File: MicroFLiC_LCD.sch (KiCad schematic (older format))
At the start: 18 parts, among them P1 2x8 pin header, P2 1x16 pin header, P3 1x16 pin socket, Q1 BCX54-16, U1 MCP4728, U2 TLV2371

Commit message: Renamed files, added part description
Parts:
- A1: value Arduino Micro -> Arduino MICRO; Alt. Order Code (none) -> Arduino MICRO; Alt. Supplier (none) -> Arduino.cc; Note (none) -> Arduino/Genuino MICRO development board; Package (none) -> Arduino MICRO; Supplier (none) -> Farnell
- C1: value 10u -> 10u/10V; Alt. Order Code (none) -> 81-GRM21BR61A106KE19; Alt. Supplier (none) -> Mouser; Note (none) -> 10μF/10V X5R 0805 ceramic capacitor; Package (none) -> 0805; Supplier (none) -> Farnell
- C2, C3: Alt. Order Code (none) -> 710-885012207098; Alt. Supplier (none) -> Mouser; Note (none) -> 100nF/50V X7R 0805 ceramic capacitor; Package (none) -> 0805; Supplier (none) -> Farnell
- LCD1: Alt. Order Code (none) -> 763-0420DZ-FL-YBW; Alt. Supplier (none) -> Mouser; Note (none) -> 20x4 character liquid crystal display; Package (none) -> 98x60mm; Supplier (none) -> Farnell
- P1: value 2x8 pin header -> 2x8 header strip; Note 2x8 pin header -> 2x8 dual header strip
- P2: value 1x16 pin header -> 1x16 header strip; Manufacturer Werth Elektronik -> Wurth Elektronik
- P3: value 1x16 pin socket -> 1x16 socket strip
- Q1: Alt. Order Code (none) -> 771-BCX54-16-T/R; Alt. Supplier (none) -> Mouser; Manufacturer NXP -> NXP Semiconductors; Note (none) -> Bipolar SOT-89 NPN transistor; Package (none) -> SOT-89; Supplier (none) -> Farnell
- R1: Alt. Order Code (none) -> 71-CRCW0805-10K-E3; Alt. Supplier (none) -> Mouser; Note (none) -> 10kΩ/1% 0805 resistor; Package (none) -> 0805; Supplier (none) -> Farnell
- R2, R3: value 18R(0.25W) -> 18R(0.5W); Alt. Order Code (none) -> 667-ERJ-P6WF18R0V; Alt. Supplier (none) -> Mouser; Note (none) -> 18Ω/1%/500mW 0805 resistor; Package (none) -> 0805; Supplier (none) -> Farnell
- U1: Alt. Order Code (none) -> 579-MCP4728-E/UN; Alt. Supplier (none) -> Mouser; Note (none) -> 12-bit quad digital-to-analog converter with EEPROM memory; Package (none) -> MSOP-10; Supplier (none) -> Farnell
- U2: Alt. Order Code (none) -> 595-TLV2371IDBVT; Alt. Supplier (none) -> Mouser; Note (none) -> 3 MHz rail-to-rail input/output operational amplifier; Package (none) -> SOT-23-5; Supplier (none) -> Farnell
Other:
- moved on the sheet: C1
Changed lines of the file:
@@
 LIBS:valves
 LIBS:jakub
-LIBS:MicroFLiC_LCD_1_0-cache
+LIBS:MicroFLiC_LCD-cache
 EELAYER 25 0
 EELAYER END
@@
 P 6100 2300
 F 0 "A1" H 6100 3300 60  0000 C CNN
-F 1 "Arduino Micro" V 6100 2300 60  0000 C CNN
+F 1 "Arduino MICRO" V 6100 2300 60  0000 C CNN
 F 2 "jakub:ArduinoMicro" V 5350 2750 60  0001 C CNN
 F 3 "" V 5350 2750 60  0000 C CNN
 F 4 "A000053" H 6100 2300 60  0001 C CNN "Part Number"
 F 5 "Arduino" H 6100 2300 60  0001 C CNN "Manufacturer"
-F 6 "2285194" H 6100 2300 60  0001 C CNN "Order Code"
+F 6 "Arduino MICRO" H 6100 2300 60  0001 C CNN "Package"
+F 7 "Farnell" H 6100 2300 60  0001 C CNN "Supplier"
+F 8 "2285194" H 6100 2300 60  0001 C CNN "Order Code"
+F 9 "Arduino.cc" H 6100 2300 60  0001 C CNN "Alt. Supplier"
+F 10 "Arduino MICRO" H 6100 2300 60  0001 C CNN "Alt. Order Code"
+F 11 "Arduino/Genuino MICRO development board" H 6100 2300 60  0001 C CNN "Note"
 	1    6100 2300
 	1    0    0    -1
@@
 P 1550 2050
 F 0 "P1" H 1550 2500 50  0000 C CNN
-F 1 "2x8 pin header" V 1550 2050 50  0000 C CNN
+F 1 "2x8 header strip" V 1550 2050 50  0000 C CNN
 F 2 "Pin_Headers:Pin_Header_Straight_2x08" H 1550 850 50  0001 C CNN
 F 3 "" H 1550 850 50  0000 C CNN
@@
 F 9 "Mouser" H 1550 2050 60  0001 C CNN "Alt. Supplier"
 F 10 "855-M20-9980845" H 1550 2050 60  0001 C CNN "Alt. Order Code"
-F 11 "2x8 pin header" H 1550 2050 60  0001 C CNN "Note"
+F 11 "2x8 dual header strip" H 1550 2050 60  0001 C CNN "Note"
 	1    1550 2050
 	1    0    0    -1
@@
 F 4 "MC42005A12W-VNMLR" H 9800 2250 60  0001 C CNN "Part Number"
 F 5 "Midas" H 9800 2250 60  0001 C CNN "Manufacturer"
-F 6 "2483355" H 9800 2250 60  0001 C CNN "Order Code"
+F 6 "98x60mm" H 9800 2250 60  0001 C CNN "Package"
+F 7 "Farnell" H 9800 2250 60  0001 C CNN "Supplier"
+F 8 "2483355" H 9800 2250 60  0001 C CNN "Order Code"
+F 9 "Mouser" H 9800 2250 60  0001 C CNN "Alt. Supplier"
+F 10 "763-0420DZ-FL-YBW" H 9800 2250 60  0001 C CNN "Alt. Order Code"
+F 11 "20x4 character liquid crystal display" H 9800 2250 60  0001 C CNN "Note"
 	1    9800 2250
 	1    0    0    -1
@@
 F 4 "MCP4728-E/UN" H 5800 4800 60  0001 C CNN "Part Number"
 F 5 "Microchip" H 5800 4800 60  0001 C CNN "Manufacturer"
-F 6 "1800217" H 5800 4800 60  0001 C CNN "Order Code"
+F 6 "MSOP-10" H 5800 4800 60  0001 C CNN "Package"
+F 7 "Farnell" H 5800 4800 60  0001 C CNN "Supplier"
+F 8 "1800217" H 5800 4800 60  0001 C CNN "Order Code"
+F 9 "Mouser" H 5800 4800 60  0001 C CNN "Alt. Supplier"
+F 10 "579-MCP4728-E/UN" H 5800 4800 60  0001 C CNN "Alt. Order Code"
+F 11 "12-bit quad digital-to-analog converter with EEPROM memory" H 5800 4800 60  0001 C CNN "Note"
 	1    5800 4800
 	1    0    0    -1
@@
 F 4 "MC0805B104K250CT" H 4800 5450 60  0001 C CNN "Part Number"
 F 5 "Multicomp" H 4800 5450 60  0001 C CNN "Manufacturer"
-F 6 "1759166" H 4800 5450 60  0001 C CNN "Order Code"
+F 6 "0805" H 4800 5450 60  0001 C CNN "Package"
+F 7 "Farnell" H 4800 5450 60  0001 C CNN "Supplier"
+F 8 "1759166" H 4800 5450 60  0001 C CNN "Order Code"
+F 9 "Mouser" H 4800 5450 60  0001 C CNN "Alt. Supplier"
+F 10 "710-885012207098" H 4800 5450 60  0001 C CNN "Alt. Order Code"
+F 11 "100nF/50V X7R 0805 ceramic capacitor" H 4800 5450 60  0001 C CNN "Note"
 	1    4800 5450
 	1    0    0    -1
@@
 L C C1
 U 1 1 566AEC7D
-P 4500 5450
-F 0 "C1" H 4525 5550 50  0000 L CNN
-F 1 "10u" H 4525 5350 50  0000 L CNN
-F 2 "Capacitors_SMD:C_0805" H 4538 5300 50  0001 C CNN
-F 3 "" H 4500 5450 50  0000 C CNN
-F 4 "GRM21BR61A106KE19L" H 4500 5450 60  0001 C CNN "Part Number"
-F 5 "Murata" H 4500 5450 60  0001 C CNN "Manufacturer"
-F 6 "1828805" H 4500 5450 60  0001 C CNN "Order Code"
-	1    4500 5450
-	1    0    0    -1
-$EndComp
-Wire Wire Line
-	4500 5800 5700 5800
+P 4300 5450
+F 0 "C1" H 4325 5550 50  0000 L CNN
+F 1 "10u/10V" H 4325 5350 50  0000 L CNN
+F 2 "Capacitors_SMD:C_0805" H 4338 5300 50  0001 C CNN
+F 3 "" H 4300 5450 50  0000 C CNN
+F 4 "GRM21BR61A106KE19L" H 4300 5450 60  0001 C CNN "Part Number"
+F 5 "Murata" H 4300 5450 60  0001 C CNN "Manufacturer"
+F 6 "0805" H 4300 5450 60  0001 C CNN "Package"
+F 7 "Farnell" H 4300 5450 60  0001 C CNN "Supplier"
+F 8 "1828805" H 4300 5450 60  0001 C CNN "Order Code"
+F 9 "Mouser" H 4300 5450 60  0001 C CNN "Alt. Supplier"
+F 10 "81-GRM21BR61A106KE19" H 4300 5450 60  0001 C CNN "Alt. Order Code"
+F 11 "10μF/10V X5R 0805 ceramic capacitor" H 4300 5450 60  0001 C CNN "Note"
+	1    4300 5450
+	1    0    0    -1
+$EndComp
+Wire Wire Line
+	4300 5800 5700 5800
 Wire Wire Line
 	4800 5800 4800 5600
@@
 	5700 5800 5800 5700
 Wire Wire Line
-	4500 5300 4500 5200
-Wire Wire Line
-	4500 5200 4800 5200
+	4300 5300 4300 5200
+Wire Wire Line
+	4300 5200 4800 5200
 Connection ~ 4800 5200
 Wire Wire Line
-	4500 5600 4500 5800
+	4300 5600 4300 5800
 Connection ~ 4800 5800
 Wire Wire Line
@@
 F 4 "MCMR08X1002FTL" V 6850 4650 60  0001 C CNN "Part Number"
 F 5 "Multicomp" V 6850 4650 60  0001 C CNN "Manufacturer"
-F 6 "2073607" V 6850 4650 60  0001 C CNN "Order Code"
+F 6 "0805" H 6850 4650 60  0001 C CNN "Package"
+F 7 "Farnell" H 6850 4650 60  0001 C CNN "Supplier"
+F 8 "2073607" V 6850 4650 60  0001 C CNN "Order Code"
+F 9 "Mouser" H 6850 4650 60  0001 C CNN "Alt. Supplier"
+F 10 "71-CRCW0805-10K-E3" H 6850 4650 60  0001 C CNN "Alt. Order Code"
+F 11 "10kΩ/1% 0805 resistor" H 6850 4650 60  0001 C CNN "Note"
 	1    6850 4650
 	0    1    1    0
@@
 F 4 "TLV2371IDBVT" H 9000 4700 60  0001 C CNN "Part Number"
 F 5 "Texas Instruments" H 9000 4700 60  0001 C CNN "Manufacturer"
-F 6 "8454990" H 9000 4700 60  0001 C CNN "Order Code"
+F 6 "SOT-23-5" H 9000 4700 60  0001 C CNN "Package"
+F 7 "Farnell" H 9000 4700 60  0001 C CNN "Supplier"
+F 8 "8454990" H 9000 4700 60  0001 C CNN "Order Code"
+F 9 "Mouser" H 9000 4700 60  0001 C CNN "Alt. Supplier"
+F 10 "595-TLV2371IDBVT" H 9000 4700 60  0001 C CNN "Alt. Order Code"
+F 11 "3 MHz rail-to-rail input/output operational amplifier" H 9000 4700 60  0001 C CNN "Note"
 	1    9000 4700
 	1    0    0    -1
@@
 P 10000 5250
 F 0 "R2" H 10050 5300 50  0000 L CNN
-F 1 "18R(0.25W)" H 10050 5200 50  0000 L CNN
+F 1 "18R(0.5W)" H 10050 5200 50  0000 L CNN
 F 2 "Resistors_SMD:R_0805" V 9930 5250 50  0001 C CNN
 F 3 "" H 10000 5250 50  0000 C CNN
 F 4 "ERJP6WF18R0V" H 10000 5250 60  0001 C CNN "Part Number"
 F 5 "Panasonic" H 10000 5250 60  0001 C CNN "Manufacturer"
-F 6 "2253864" H 10000 5250 60  0001 C CNN "Order Code"
+F 6 "0805" H 10000 5250 60  0001 C CNN "Package"
+F 7 "Farnell" H 10000 5250 60  0001 C CNN "Supplier"
+F 8 "2253864" H 10000 5250 60  0001 C CNN "Order Code"
+F 9 "Mouser" H 10000 5250 60  0001 C CNN "Alt. Supplier"
+F 10 "667-ERJ-P6WF18R0V" H 10000 5250 60  0001 C CNN "Alt. Order Code"
+F 11 "18Ω/1%/500mW 0805 resistor" H 10000 5250 60  0001 C CNN "Note"
 	1    10000 5250
 	1    0    0    -1
@@
 F 3 "" H 9900 4700 50  0000 C CNN
 F 4 "BCX54-16" H 9900 4700 60  0001 C CNN "Part Number"
-F 5 "NXP" H 9900 4700 60  0001 C CNN "Manufacturer"
-F 6 "8734950" H 9900 4700 60  0001 C CNN "Order Code"
+F 5 "NXP Semiconductors" H 9900 4700 60  0001 C CNN "Manufacturer"
+F 6 "SOT-89" H 9900 4700 60  0001 C CNN "Package"
+F 7 "Farnell" H 9900 4700 60  0001 C CNN "Supplier"
+F 8 "8734950" H 9900 4700 60  0001 C CNN "Order Code"
+F 9 "Mouser" H 9900 4700 60  0001 C CNN "Alt. Supplier"
+F 10 "771-BCX54-16-T/R" H 9900 4700 60  0001 C CNN "Alt. Order Code"
+F 11 "Bipolar SOT-89 NPN transistor" H 9900 4700 60  0001 C CNN "Note"
 	1    9900 4700
 	1    0    0    -1
@@
 F 4 "MC0805B104K250CT" H 8100 4850 60  0001 C CNN "Part Number"
 F 5 "Multicomp" H 8100 4850 60  0001 C CNN "Manufacturer"
-F 6 "1759166" H 8100 4850 60  0001 C CNN "Order Code"
+F 6 "0805" H 8100 4850 60  0001 C CNN "Package"
+F 7 "Farnell" H 8100 4850 60  0001 C CNN "Supplier"
+F 8 "1759166" H 8100 4850 60  0001 C CNN "Order Code"
+F 9 "Mouser" H 8100 4850 60  0001 C CNN "Alt. Supplier"
+F 10 "710-885012207098" H 8100 4850 60  0001 C CNN "Alt. Order Code"
+F 11 "100nF/50V X7R 0805 ceramic capacitor" H 8100 4850 60  0001 C CNN "Note"
 	1    8100 4850
 	1    0    0    -1
@@
 P 10000 5650
 F 0 "R3" H 10050 5700 50  0000 L CNN
-F 1 "18R(0.25W)" H 10050 5600 50  0000 L CNN
+F 1 "18R(0.5W)" H 10050 5600 50  0000 L CNN
 F 2 "Resistors_SMD:R_0805" V 9930 5650 50  0001 C CNN
 F 3 "" H 10000 5650 50  0000 C CNN
 F 4 "ERJP6WF18R0V" H 10000 5650 60  0001 C CNN "Part Number"
 F 5 "Panasonic" H 10000 5650 60  0001 C CNN "Manufacturer"
-F 6 "2253864" H 10000 5650 60  0001 C CNN "Order Code"
+F 6 "0805" H 10000 5650 60  0001 C CNN "Package"
+F 7 "Farnell" H 10000 5650 60  0001 C CNN "Supplier"
+F 8 "2253864" H 10000 5650 60  0001 C CNN "Order Code"
+F 9 "Mouser" H 10000 5650 60  0001 C CNN "Alt. Supplier"
+F 10 "667-ERJ-P6WF18R0V" H 10000 5650 60  0001 C CNN "Alt. Order Code"
+F 11 "18Ω/1%/500mW 0805 resistor" H 10000 5650 60  0001 C CNN "Note"
 	1    10000 5650
 	1    0    0    -1
@@
 P 10600 2250
 F 0 "P2" H 10600 3100 50  0000 C CNN
-F 1 "1x16 pin header" V 10700 2250 50  0000 C CNN
+F 1 "1x16 header strip" V 10700 2250 50  0000 C CNN
 F 2 "" H 10600 2250 50  0000 C CNN
 F 3 "" H 10600 2250 50  0000 C CNN
 F 4 "61301611121" H 10600 2250 60  0001 C CNN "Part Number"
-F 5 "Werth Elektronik" H 10600 2250 60  0001 C CNN "Manufacturer"
+F 5 "Wurth Elektronik" H 10600 2250 60  0001 C CNN "Manufacturer"
 F 6 "SIL-16" H 10600 2250 60  0001 C CNN "Package"
 F 7 "Farnell" H 10600 2250 60  0001 C CNN "Supplier"
@@
 P 11000 2250
 F 0 "P3" H 11000 3100 50  0000 C CNN
-F 1 "1x16 pin socket" V 11100 2250 50  0000 C CNN
+F 1 "1x16 socket strip" V 11100 2250 50  0000 C CNN
 F 2 "" H 11000 2250 50  0000 C CNN
 F 3 "" H 11000 2250 50  0000 C CNN

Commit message: Fixed LCD part description
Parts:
- LCD1: Package 98x60mm -> 98mm×60mm
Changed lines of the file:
@@
 F 4 "MC42005A12W-VNMLR" H 9800 2250 60  0001 C CNN "Part Number"
 F 5 "Midas" H 9800 2250 60  0001 C CNN "Manufacturer"
-F 6 "98x60mm" H 9800 2250 60  0001 C CNN "Package"
+F 6 "98mm×60mm" H 9800 2250 60  0001 C CNN "Package"
 F 7 "Farnell" H 9800 2250 60  0001 C CNN "Supplier"
 F 8 "2483355" H 9800 2250 60  0001 C CNN "Order Code"

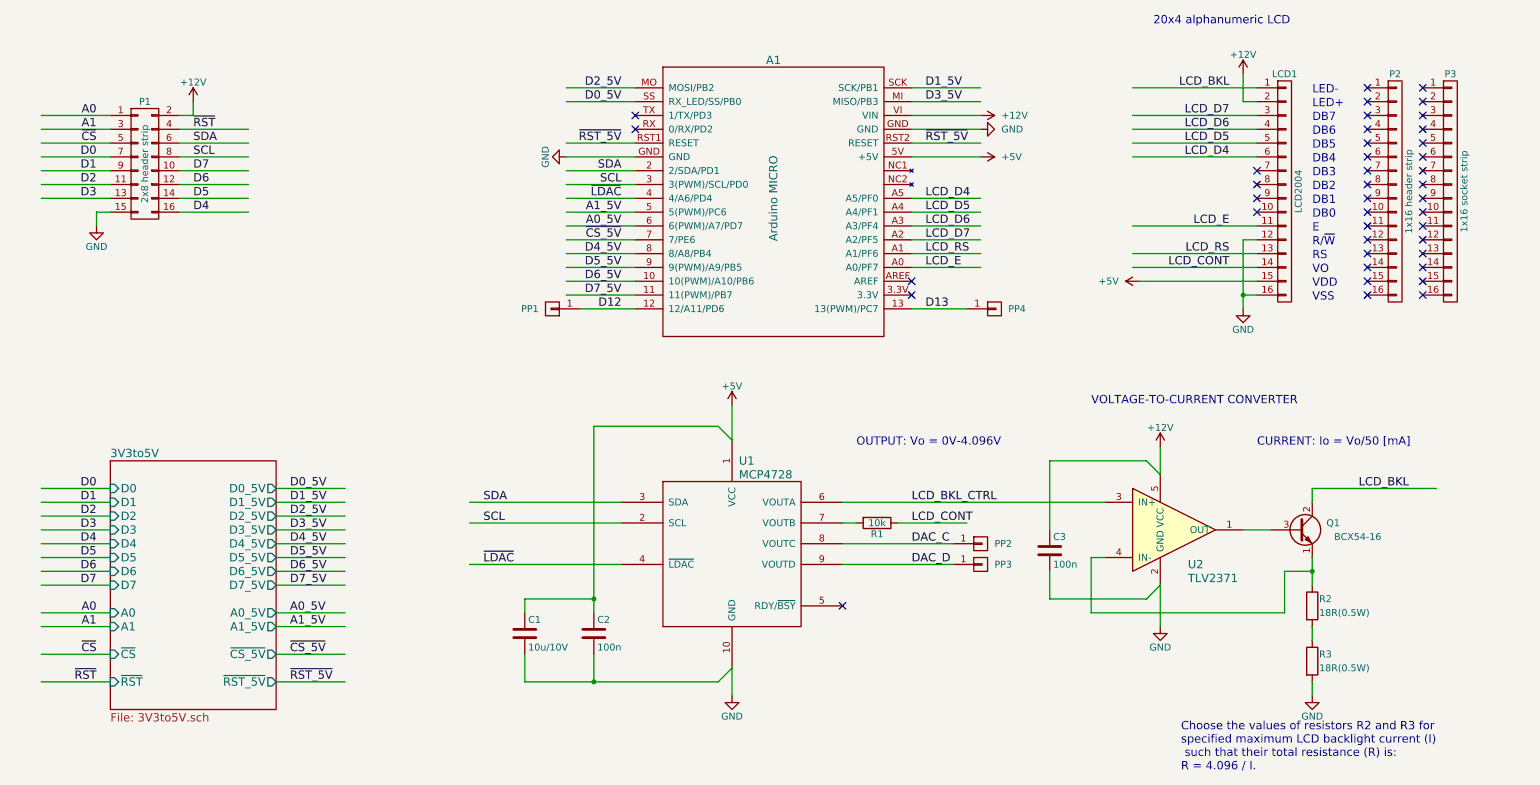
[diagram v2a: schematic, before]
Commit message: Fixed LCD orientation, added powerful emitter-follower amplifier
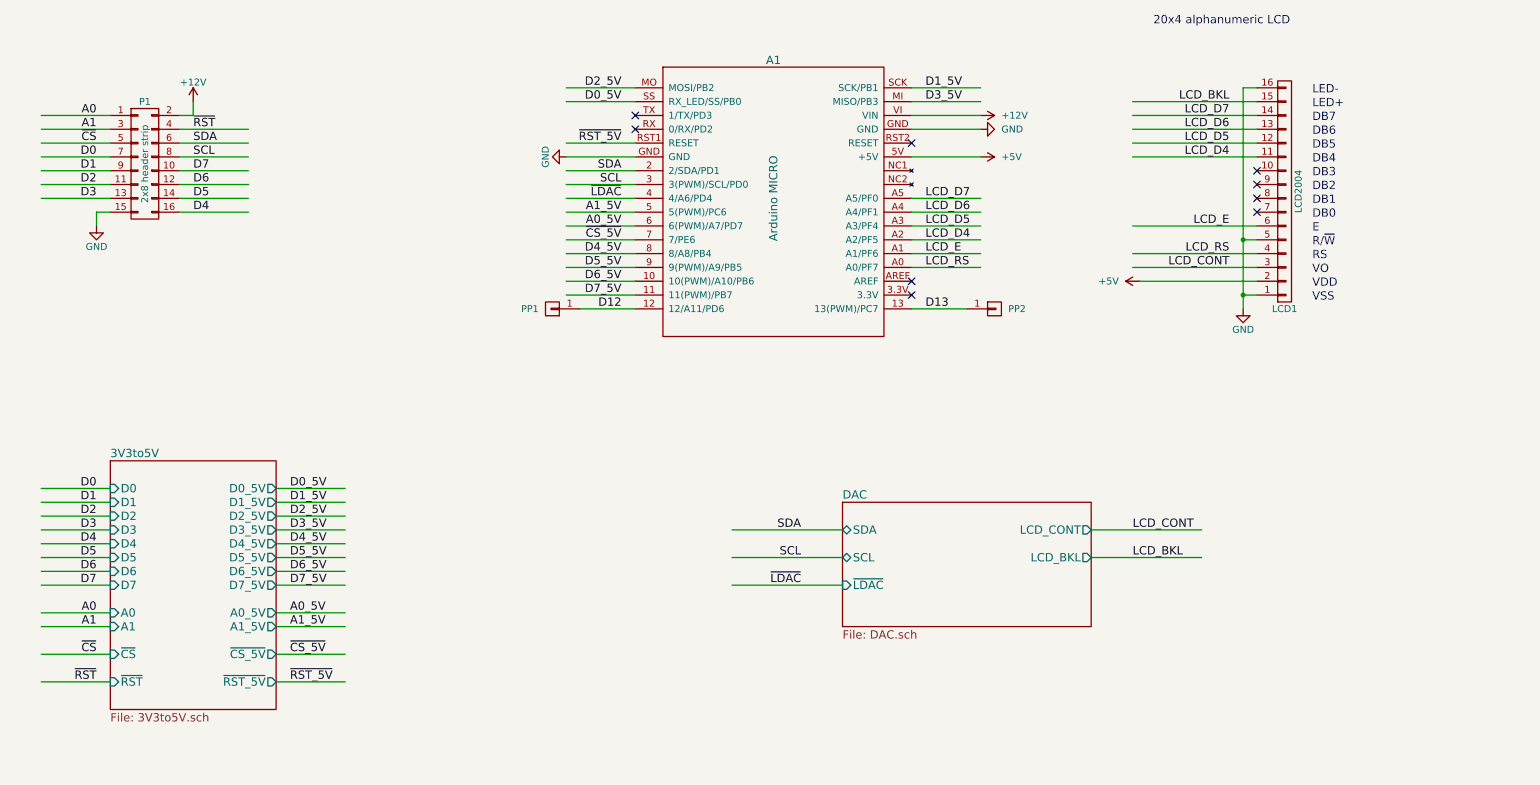
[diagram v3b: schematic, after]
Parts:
- removed C1: 10u/10V, Capacitors_SMD:C_0805, symbol C
- removed C2, C3: 100n, Capacitors_SMD:C_0805, symbol C
- removed P2: 1x16 header strip, symbol CONN_01X16
- removed P3: 1x16 socket strip, symbol CONN_01X16
- removed PP2, PP3: CONN_01X01, jakub:PIN_ARRAY_1, symbol CONN_01X01
- removed Q1: BCX54-16, TO_SOT_Packages_SMD:SOT89-3_Housing, symbol Q_NPN_ECB
- removed R1: 10k, Resistors_SMD:R_0805, symbol R
- removed R2, R3: 18R(0.5W), Resistors_SMD:R_0805, symbol R
- removed U1: MCP4728, Housings_SSOP:MSOP-10_3x3mm_Pitch0.5mm, symbol MCP4728
- removed U2: TLV2371, TO_SOT_Packages_SMD:SOT-23-5, symbol TLV2371xDBV
- renumbered PP4 to PP2
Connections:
- net labels removed: DAC_C, DAC_D, LCD_BKL_CTRL
- wire segments 122 -> 87
- no-connect marks 41 -> 9
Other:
- note removed: "CURRENT: Io = Vo/50 [mA]"
- note removed: "Choose the values of resistors R2 and R3 for\nspecified maximum LCD backlight current (I)\n such that their total resistance (R) is:\nR = 4.096 / I."
- note removed: "OUTPUT: Vo = 0V-4.096V"
- note removed: "VOLTAGE-TO-CURRENT CONVERTER"

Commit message: Finalized PCB for production
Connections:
- wire segments 87 -> 91
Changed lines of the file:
@@
 D3
 Wire Wire Line
-	1300 2400 1200 2400
+	800  2400 1300 2400
 Wire Wire Line
 	1800 1800 2300 1800
@@
 	1200 2400 1200 2500
 Wire Wire Line
-	1800 1700 1900 1700
+	1800 1700 2300 1700
 Wire Wire Line
 	1900 1700 1900 1600
@@
 $EndComp
 Wire Wire Line
-	7600 2000 7100 2000
+	7100 2000 7600 2000
 $Comp
 L +5V #PWR06
@@
 LCD_BKL
 NoConn ~ 7100 1900
+Wire Wire Line
+	2300 1700 2300 1600
+Connection ~ 1900 1700
+Wire Wire Line
+	800  2400 800  2500
+Connection ~ 1200 2400
+$Comp
+L PWR_FLAG #FLG09
+U 1 1 56F28A7D
+P 2300 1600
+F 0 "#FLG09" H 2300 1695 50  0001 C CNN
+F 1 "PWR_FLAG" H 2300 1780 50  0000 C CNN
+F 2 "" H 2300 1600 50  0000 C CNN
+F 3 "" H 2300 1600 50  0000 C CNN
+	1    2300 1600
+	1    0    0    -1
+$EndComp
+$Comp
+L PWR_FLAG #FLG010
+U 1 1 56F28C01
+P 800 2500
+F 0 "#FLG010" H 800 2595 50  0001 C CNN
+F 1 "PWR_FLAG" H 800 2680 50  0000 C CNN
+F 2 "" H 800 2500 50  0000 C CNN
+F 3 "" H 800 2500 50  0000 C CNN
+	1    800  2500
+	-1   0    0    1
+$EndComp
+$Comp
+L PWR_FLAG #FLG011
+U 1 1 56F2918A
+P 7600 2150
+F 0 "#FLG011" H 7600 2245 50  0001 C CNN
+F 1 "PWR_FLAG" V 7600 2350 50  0000 L CNN
+F 2 "" H 7600 2150 50  0000 C CNN
+F 3 "" H 7600 2150 50  0000 C CNN
+	1    7600 2150
+	0    1    1    0
+$EndComp
+Wire Wire Line
+	7600 2150 7250 2150
+Wire Wire Line
+	7250 2150 7250 2000
+Connection ~ 7250 2000
 $EndSCHEMATC
